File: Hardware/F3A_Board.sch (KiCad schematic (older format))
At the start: 14 parts, among them J1 Conn_01x03, Q1 BC550, Q2 BC550, U1 W25Q64V

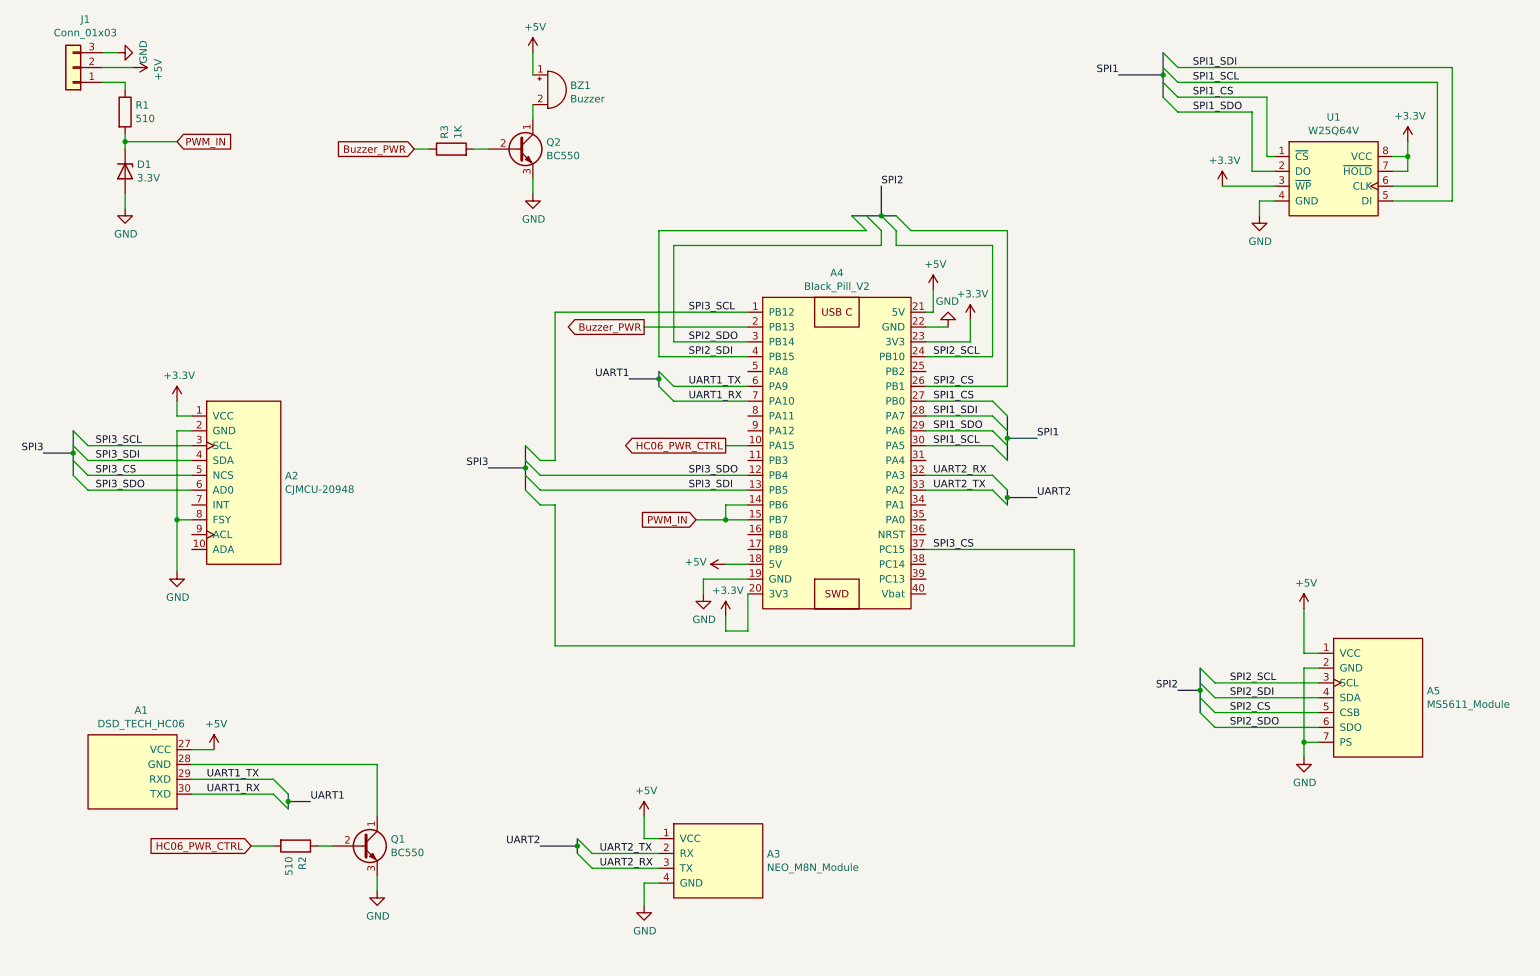
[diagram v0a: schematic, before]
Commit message: Changing pin labels
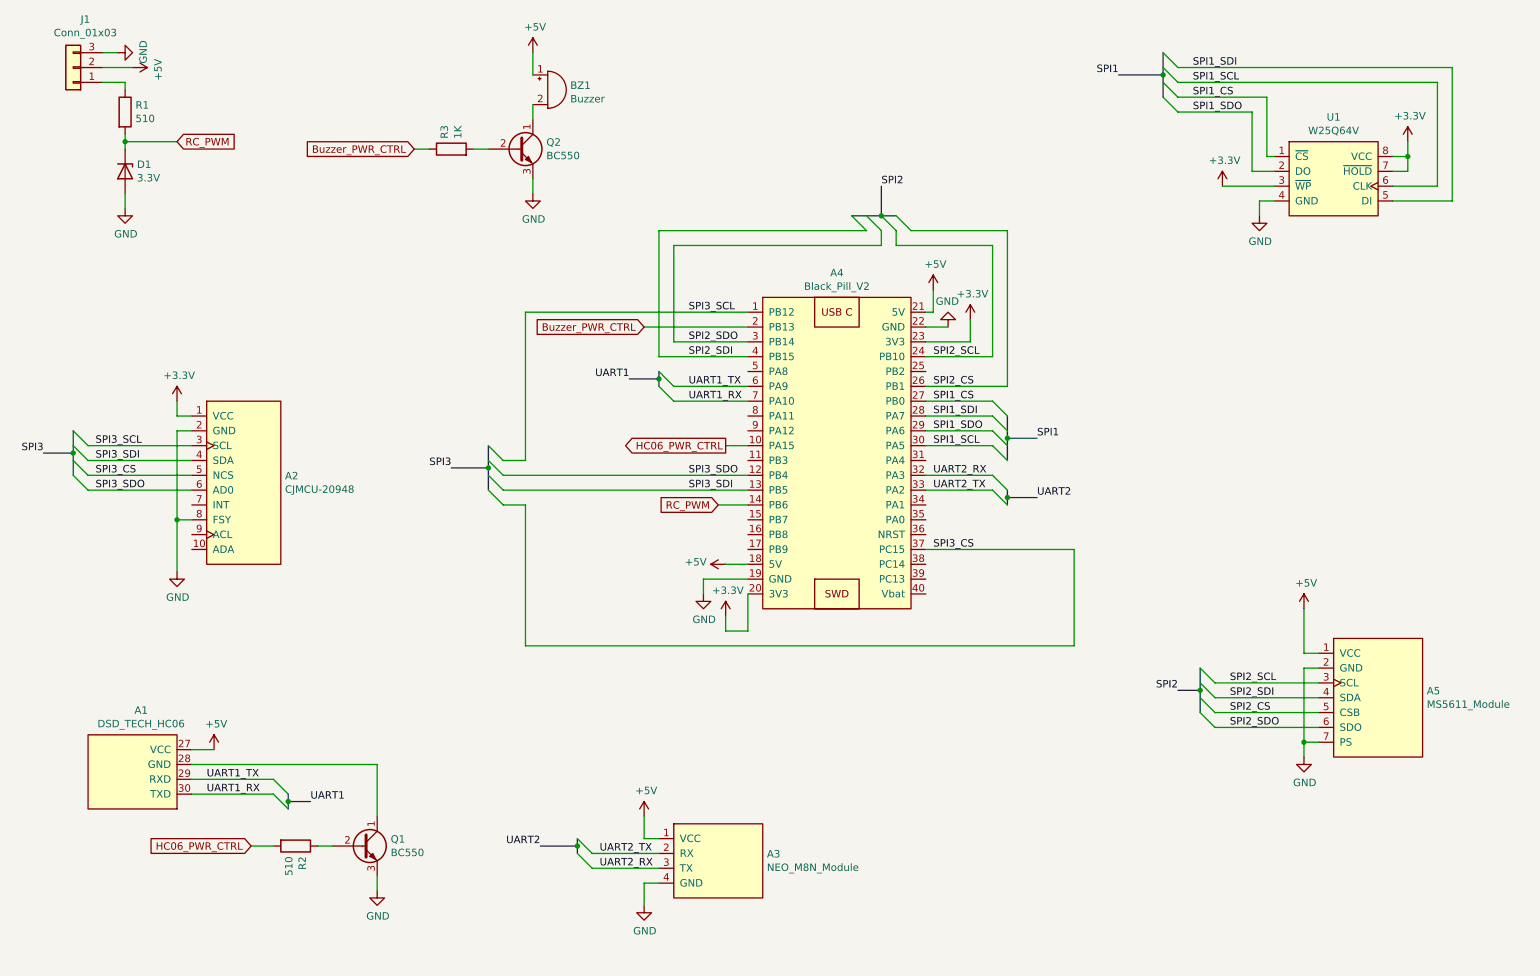
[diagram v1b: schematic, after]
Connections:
- net Buzzer_PWR renamed Buzzer_PWR_CTRL
- net PWM_IN renamed RC_PWM
- net RC_PWM: no longer A4.15 (PB7)
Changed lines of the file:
@@
 UART1
 Entry Wire Line
-	4150 3850 4250 3950
-Entry Wire Line
-	4150 3950 4250 4050
-Entry Wire Line
-	4150 4050 4250 4150
-Entry Wire Line
-	4150 3750 4250 3850
-Wire Wire Line
-	4350 2850 4350 3850
-Wire Wire Line
-	4350 3850 4250 3850
-Wire Wire Line
-	4250 4150 4350 4150
-Wire Wire Line
-	4350 4150 4350 5100
+	3900 3850 4000 3950
+Entry Wire Line
+	3900 3950 4000 4050
+Entry Wire Line
+	3900 4050 4000 4150
+Entry Wire Line
+	3900 3750 4000 3850
+Wire Wire Line
+	4150 2850 4150 3850
+Wire Wire Line
+	4150 4150 4150 5100
 Wire Wire Line
 	7850 5100 7850 4450
@@
 	7850 4450 6850 4450
 Wire Bus Line
-	4150 3900 3900 3900
-Connection ~ 4150 3900
-Text Label 3900 3900 2    50   ~ 0
+	3900 3900 3650 3900
+Connection ~ 3900 3900
+Text Label 3650 3900 2    50   ~ 0
 SPI3
 Wire Wire Line
@@
 	-1   0    0    1
 $EndComp
-Wire Wire Line
-	5650 4150 5500 4150
-Wire Wire Line
-	5500 4150 5500 4250
-Wire Wire Line
-	5500 4250 5650 4250
 $Comp
 L Device:D_Zener D1
@@
 	1450 1700 1450 1750
 Text GLabel 1800 1700 2    50   Input ~ 0
-PWM_IN
-Text GLabel 5300 4250 0    50   Input ~ 0
-PWM_IN
-Wire Wire Line
-	5300 4250 5500 4250
-Connection ~ 5500 4250
+RC_PWM
+Text GLabel 5450 4150 0    50   Input ~ 0
+RC_PWM
 $Comp
 L Device:Buzzer BZ1
@@
 Wire Wire Line
 	3800 1750 3900 1750
-Text GLabel 4950 2950 0    50   Output ~ 0
-Buzzer_PWR
-Wire Wire Line
-	4350 2850 5650 2850
-Wire Wire Line
-	4250 3950 5650 3950
-Wire Wire Line
-	4250 4050 5650 4050
-Wire Wire Line
-	4350 5100 7850 5100
 Wire Wire Line
 	5650 2950 4950 2950
 Text GLabel 3400 1750 0    50   Input ~ 0
-Buzzer_PWR
+Buzzer_PWR_CTRL
 Wire Wire Line
 	3400 1750 3500 1750
+Text GLabel 4950 2950 0    50   Input ~ 0
+Buzzer_PWR_CTRL
+Wire Wire Line
+	4000 3850 4150 3850
+Wire Wire Line
+	4000 3950 5650 3950
+Wire Wire Line
+	4000 4050 5650 4050
+Wire Wire Line
+	4000 4150 4150 4150
+Wire Wire Line
+	4150 2850 5650 2850
+Wire Wire Line
+	4150 5100 7850 5100
+Wire Wire Line
+	5650 4150 5450 4150
 Wire Bus Line
 	6350 2200 6550 2200
@@
 	8700 5400 8700 5550
 Wire Bus Line
-	4150 3750 4150 3900
-Wire Bus Line
-	4150 3900 4150 4050
+	3900 3750 3900 3900
+Wire Bus Line
+	3900 3900 3900 4050
 Wire Bus Line
 	1100 3650 1100 3800

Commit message: HC06 now controlled with high side switch
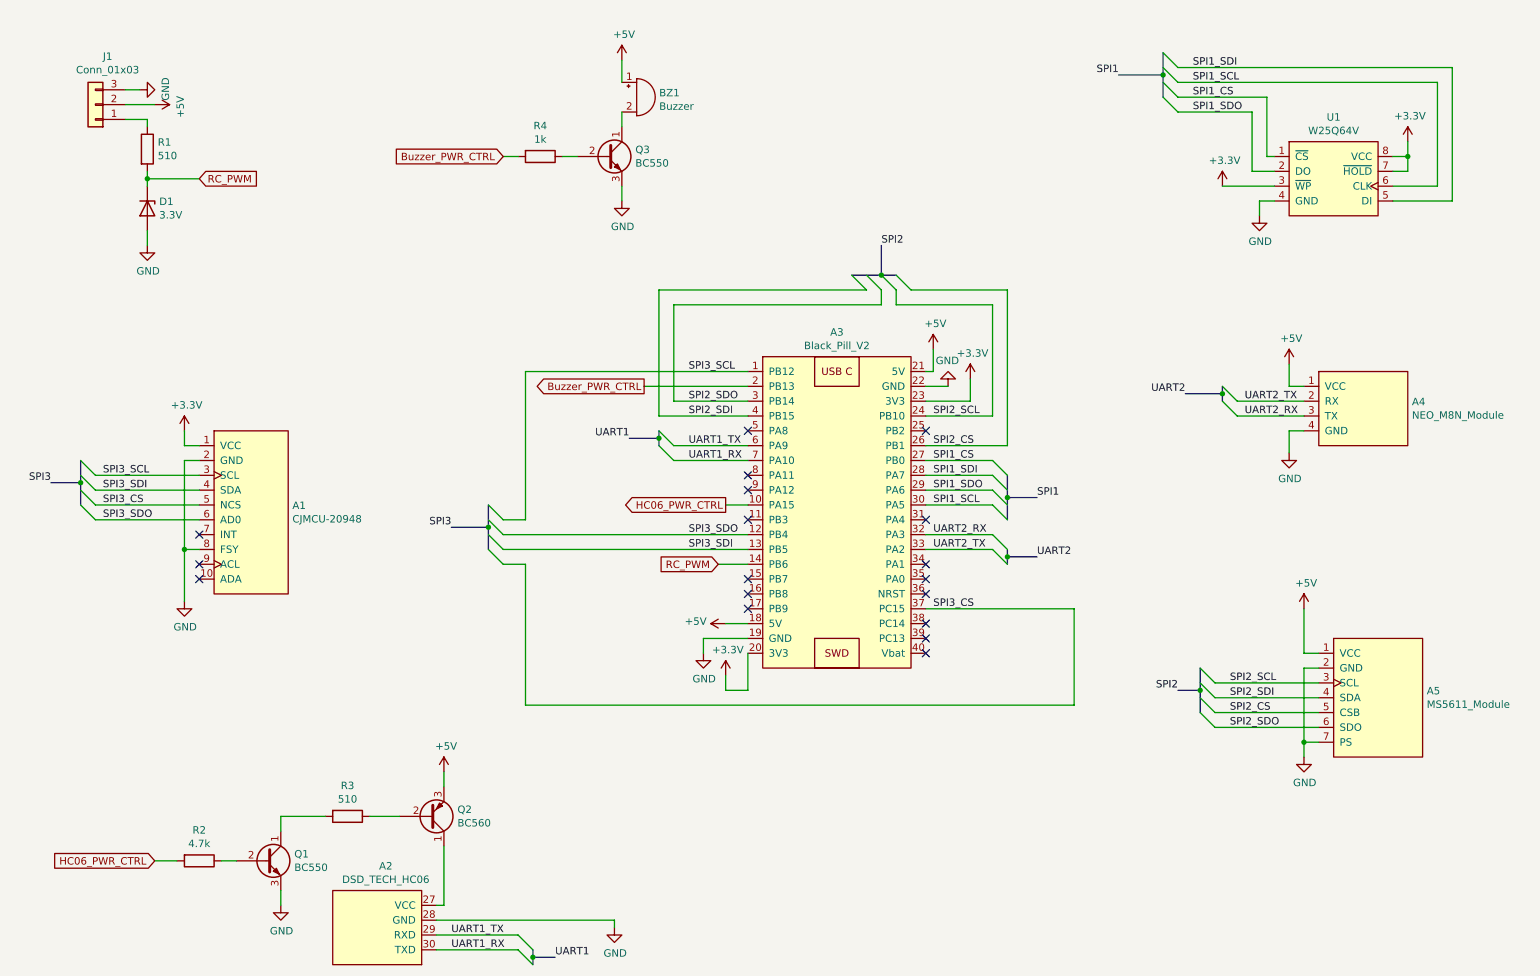
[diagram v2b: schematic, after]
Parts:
- added Q2: BC560, Package_TO_SOT_THT:TO-92S_Wide, symbol Transistor_BJT:BC560
- added R4: 1k, symbol Device:R
- R2: value 510 -> 4.7k; footprint Resistor_THT:R_Axial_DIN0204_L3.6mm_D1.6mm_P7.62mm_Horizontal -> (none)
- R3: value 1K -> 510
- renumbered A2 to A1, A1 to A2, A4 to A3, A3 to A4, Q2 to Q3
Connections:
- net +5V: now also Q2.3 (E); no longer A2.27 (VCC)
- net Buzzer_PWR_CTRL: now also R4.2; no longer R3.1
- net GND: now also A2.28 (GND)
- net at Q1.1 (C): now also R3.2; no longer A2.28 (GND)
- net at Q3.2 (B): now also R4.1; no longer R3.2
- new net: A2.27 (VCC), Q2.1 (C)
- new net: Q2.2 (B), R3.1
- no-connect marks 0 -> 18
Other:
- moved on the sheet: A1, A2, A3, A4, BZ1, D1, J1, Q1, Q3, R1
